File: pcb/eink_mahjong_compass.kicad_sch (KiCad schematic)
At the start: 24 parts, among them Q1 C10487, U2 C85364, U3 ESP32-S3-MINI, U8 C235316

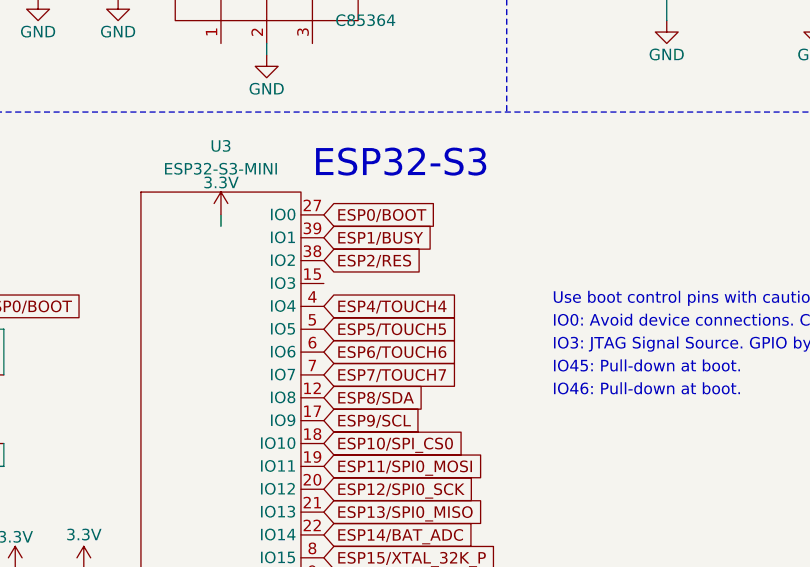
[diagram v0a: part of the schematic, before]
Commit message: pcb: add missing trace to make deep sleep wakeup work
Connect button 4 for gpio 3 as well, so it can be used to wake up the
esp32 from deep sleep as the gpios selected for the buttons don't have
that capability.
In a future revision this should be redesigned so all buttons can act as
wakeup trigger.
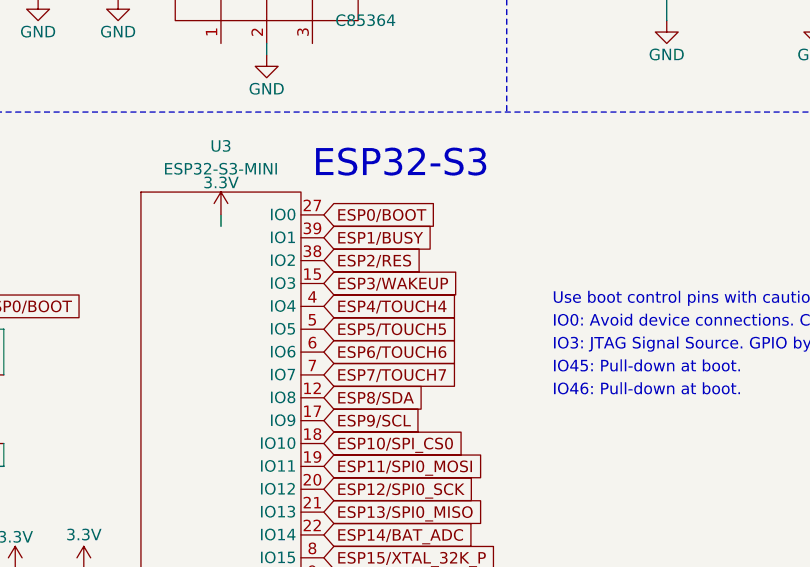
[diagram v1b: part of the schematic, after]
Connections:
- net ESP3/WAKEUP: now reaches U3.15 (IO3)
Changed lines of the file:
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@@
+		)
+	)
+	(global_label "ESP3{slash}WAKEUP"
+		(shape input)
+		(at 74.93 96.52 0)
+		(fields_autoplaced yes)
+		(effects
+			(font
+				(size 1.27 1.27)
+			)
+			(justify left)
+		)
+		(property "Intersheetrefs" "${INTERSHEET_REFS}"
+			(at 91.6432 96.52 0)
+			(hide yes)
+			(show_name no)
+			(do_not_autoplace no)
+			(effects
+				(font
+					(size 1.27 1.27)
+				)
+				(justify left)
+			)
 		)
 	)
